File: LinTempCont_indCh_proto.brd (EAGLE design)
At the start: 76.2 x 34.3 mm, 26 parts

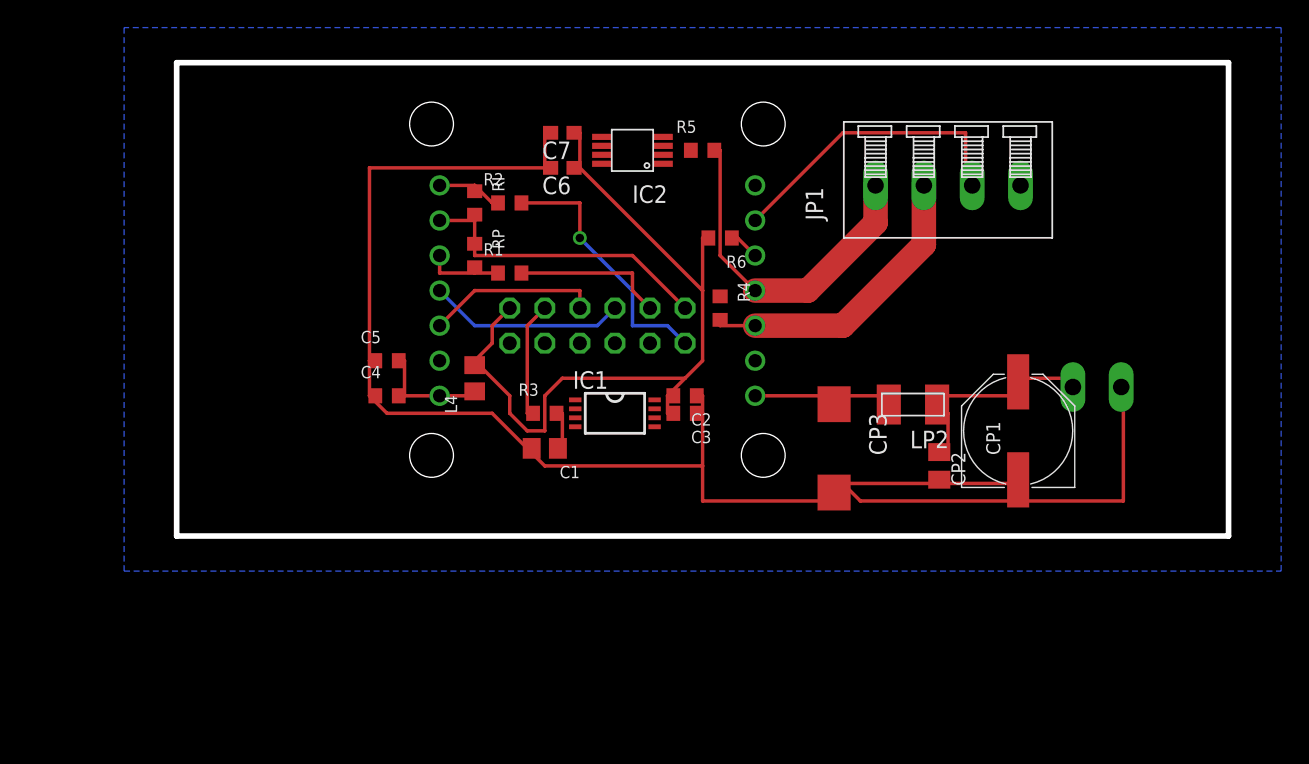
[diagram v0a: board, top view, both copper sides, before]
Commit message: Schematic updates and progress routing both boards
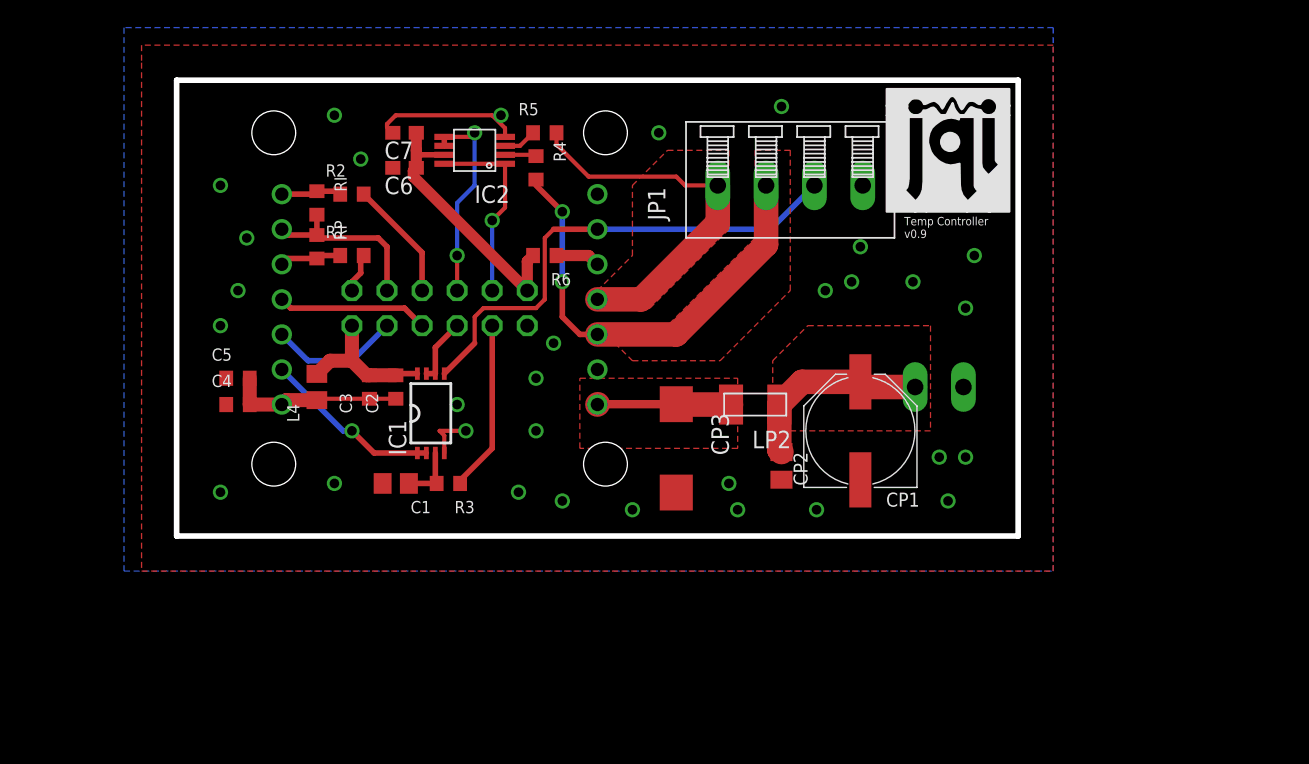
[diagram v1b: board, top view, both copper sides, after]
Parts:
- added U$1: (no value), JQI_Logo:JQI_LOGO_NEGATIVE-SILKSCREEN
- moved C3 22.9 mm to (14.0, 10.8), turned to 90 degrees
- moved C2 21.0 mm to (15.9, 10.8), turned to 90 degrees
- moved R4 16.8 mm to (26.0, 26.7)
- moved IC1 13.3 mm to (18.4, 8.89), turned to 90 degrees
- moved R6 12.8 mm to (26.7, 20.3)
- moved JP3 11.5 mm to (19.1, 16.5)
- moved R1 11.5 mm to (12.7, 20.3)
- moved R5 11.5 mm to (26.7, 29.2)
- moved L4 11.4 mm to (10.2, 10.8)
- moved R2 11.4 mm to (12.7, 24.8)
- moved RP 11.4 mm to (10.2, 21.0)
- moved U1 11.4 mm to (19.1, 17.1)
- moved LP2 11.4 mm to (41.9, 9.53)
- moved IC2 11.4 mm to (21.6, 27.9)
- moved C6 11.4 mm to (16.5, 26.7)
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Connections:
- net +1V: now also JP3.3; no longer JP3.11
- net 2.5V: now also JP3.9; no longer JP3.10
- net ACT_T: now also JP3.8; no longer JP3.6
- net AGND: now also JP3.12; no longer JP3.2
- net I: now also JP3.5; no longer JP3.12
- net LIMA: now also JP3.4; no longer JP3.5
- net LIMB: now also JP3.6; no longer JP3.7
- net P: now also JP3.1; no longer JP3.9
- net VDD: now also JP3.11, JP3.2; no longer JP3.1
- net VMON: now also JP3.7; no longer JP3.8
- net VSET: now also JP3.10; no longer JP3.3
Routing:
- net AGND: track 121.3 -> 20.1 mm, vias 0 -> 31
- net VDD: track 57.3 -> 30.5 mm
- net VMON: track 0.00 -> 14.9 mm, vias 0 -> 2
- net N$2: track 22.2 -> 36.2 mm
- net 2.5V: track 0.00 -> 14.0 mm, vias 0 -> 1
- net N$7: track 0.00 -> 13.0 mm, vias 0 -> 1
- net OUTB: track 21.9 -> 33.0 mm, vias 0 -> 2
- net I: track 19.0 -> 8.74 mm, vias 1 -> 0
- net +1V: track 22.3 -> 12.8 mm
- net P: track 11.1 -> 2.89 mm
- net ACT_T: track 0.00 -> 4.78 mm
- net VSET: track 8.57 -> 12.4 mm
- net LIMB: track 14.3 -> 10.9 mm
- net LIMA: track 12.5 -> 9.46 mm
- net N$16: track 0.00 -> 2.42 mm
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- added copper zone on layer 1, net AGND
- added copper zone on layer 1, net OUTA
- added copper zone on layer 1, net OUTB
- added copper zone on layer 1, net V+
- added copper zone on layer 1, net VSS
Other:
- board size 76.2 x 34.3 mm -> 61 x 33 mm
- board text added: "Temp Controller v0.9"

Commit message: Board/Schematic updates and tweaks
Incorporate suggestions from Neal and Alessandro
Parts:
- added C8: 100nF, rlc-jqi:0603
- added RSG: DNP, rlc-jqi:0603
- R6: device rlc-jqi:0603 -> jqi_passives:R_0805
- moved RI 6.38 mm to (3.81, 24.8)
- moved RP 6.38 mm to (3.81, 20.3)
- moved R1 0.90 mm to (12.1, 21.0)
- moved R2 0.63 mm to (12.1, 24.8)
- moved R6 0.63 mm to (26.7, 21.0)
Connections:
- new net N$6: RSG.2, U1.P$8
- net AGND: now also C8.1, RSG.1
- net N$2: now also C8.2
- net N$4: now also R6.P$1; no longer R6.1
- net VDD: now also R6.P$2; no longer R6.2
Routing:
- net +1V: track 12.8 -> 19.1 mm
- net N$2: track 36.2 -> 41.1 mm
- net AGND: track 20.1 -> 15.5 mm
- net N$3: track 4.41 -> 8.72 mm
- net N$1: track 4.49 -> 8.59 mm
- net I: track 8.74 -> 10.7 mm
- net VDD: track 30.5 -> 31.1 mm
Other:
- board text added: "Temp Controller v0.9 BJR"
- board text removed: "Temp Controller v0.9"

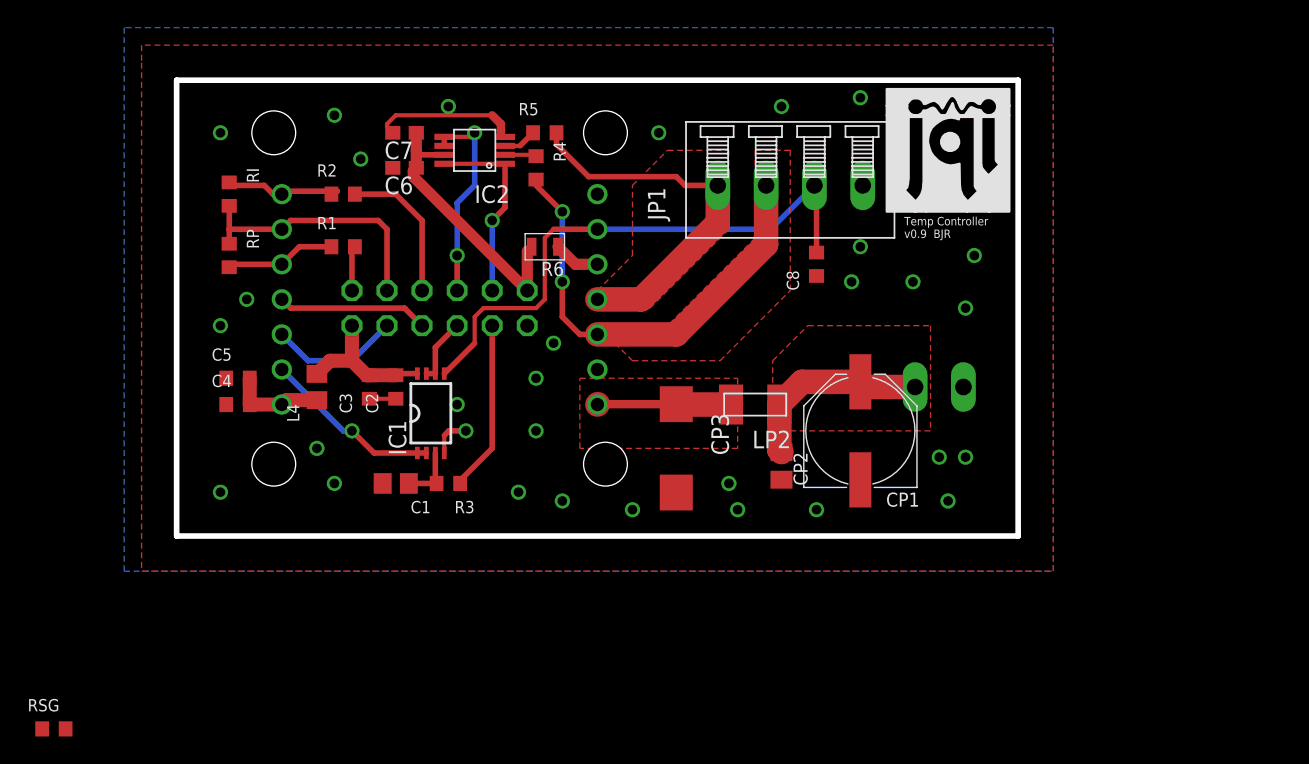
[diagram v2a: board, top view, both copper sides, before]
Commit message: Board/Schematic Clean up-lcd.init tweak
Added encoder hold event to initialize LCD to try to get around bug
where LCD display goes blank. The bug appears to be from a loose solder
connection on first prototype
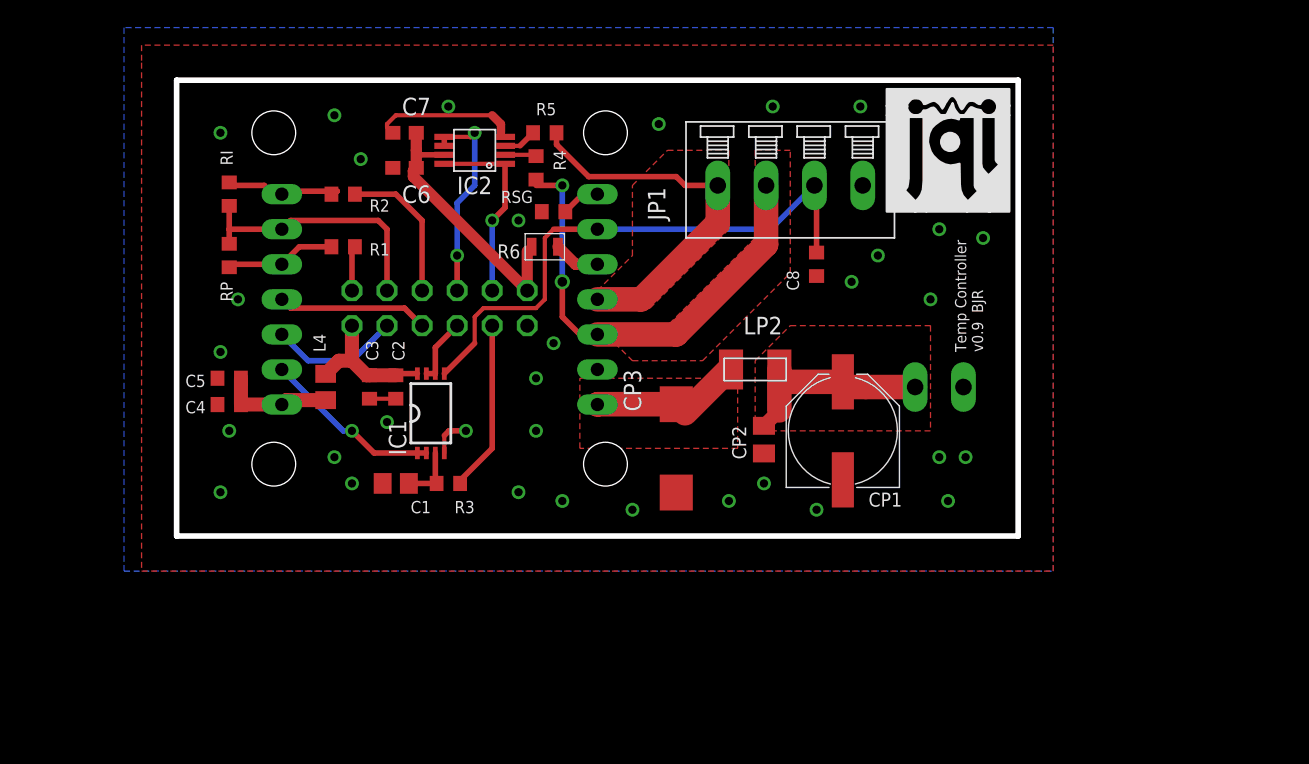
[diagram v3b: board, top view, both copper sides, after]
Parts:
- moved RSG 52.1 mm to (27.3, 23.5)
- moved LP2 2.54 mm to (41.9, 12.1)
- moved CP2 2.29 mm to (42.5, 6.99)
- moved CP1 1.27 mm to (48.3, 7.62)
- moved C4 0.64 mm to (3.81, 9.53)
- moved C5 0.64 mm to (3.81, 11.4)
- moved L4 0.63 mm to (10.8, 10.8)
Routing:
- net N$6: track 0.00 -> 2.85 mm
- net VSS: track 9.70 -> 11.3 mm
- net N$26: track 6.90 -> 8.17 mm
- net OUTB: track 33.0 -> 34.1 mm
- net V+: track 14.2 -> 14.9 mm
- net VDD: track 31.1 -> 30.5 mm
- net AGND: vias 31 -> 33

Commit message: Add DAC Vref Jumper/Silkscreen Cleanup
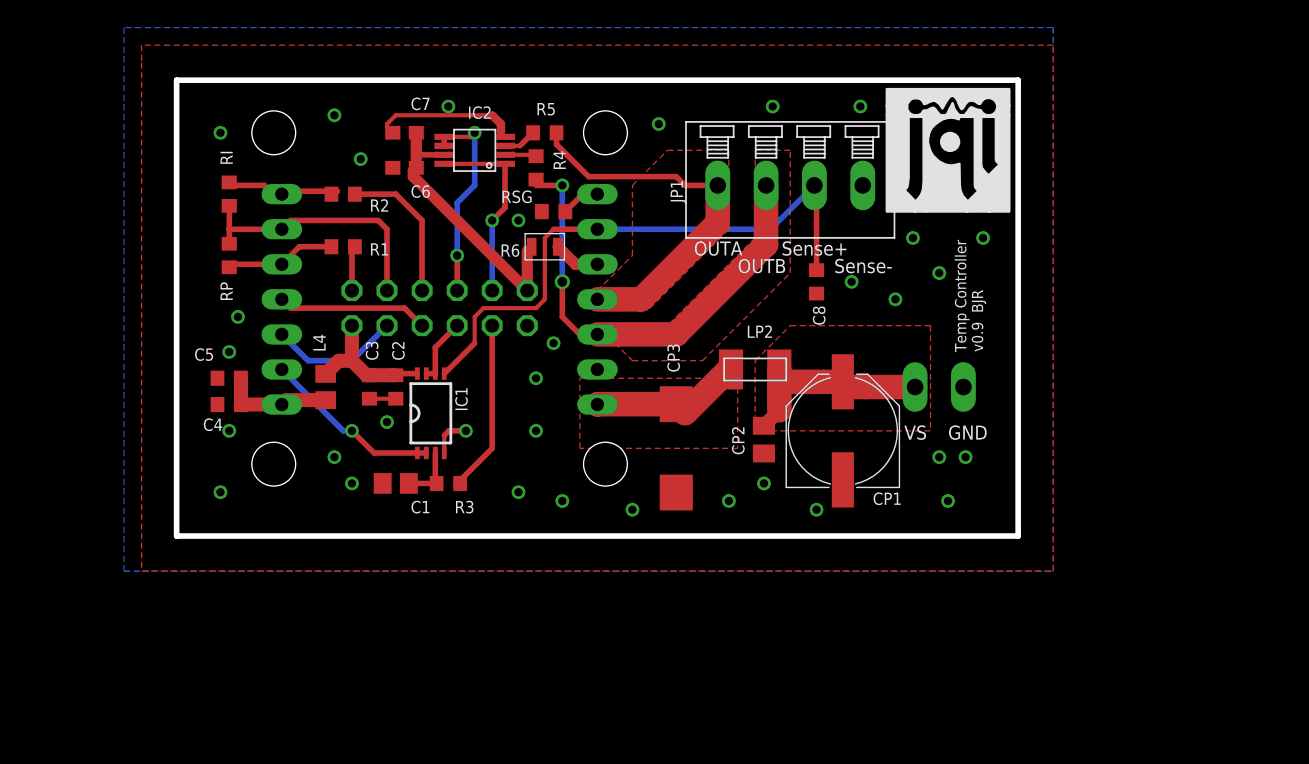
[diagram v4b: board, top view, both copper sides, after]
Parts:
- moved C8 1.27 mm to (46.4, 18.4)
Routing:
- net N$2: track 41.1 -> 42.4 mm
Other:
- board text added: "GND"
- board text added: "OUTA"
- board text added: "OUTB"
- board text added: "Sense+"
- board text added: "Sense-"
- board text added: "VS"

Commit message: Add BOM, minor updates to reflect part availability
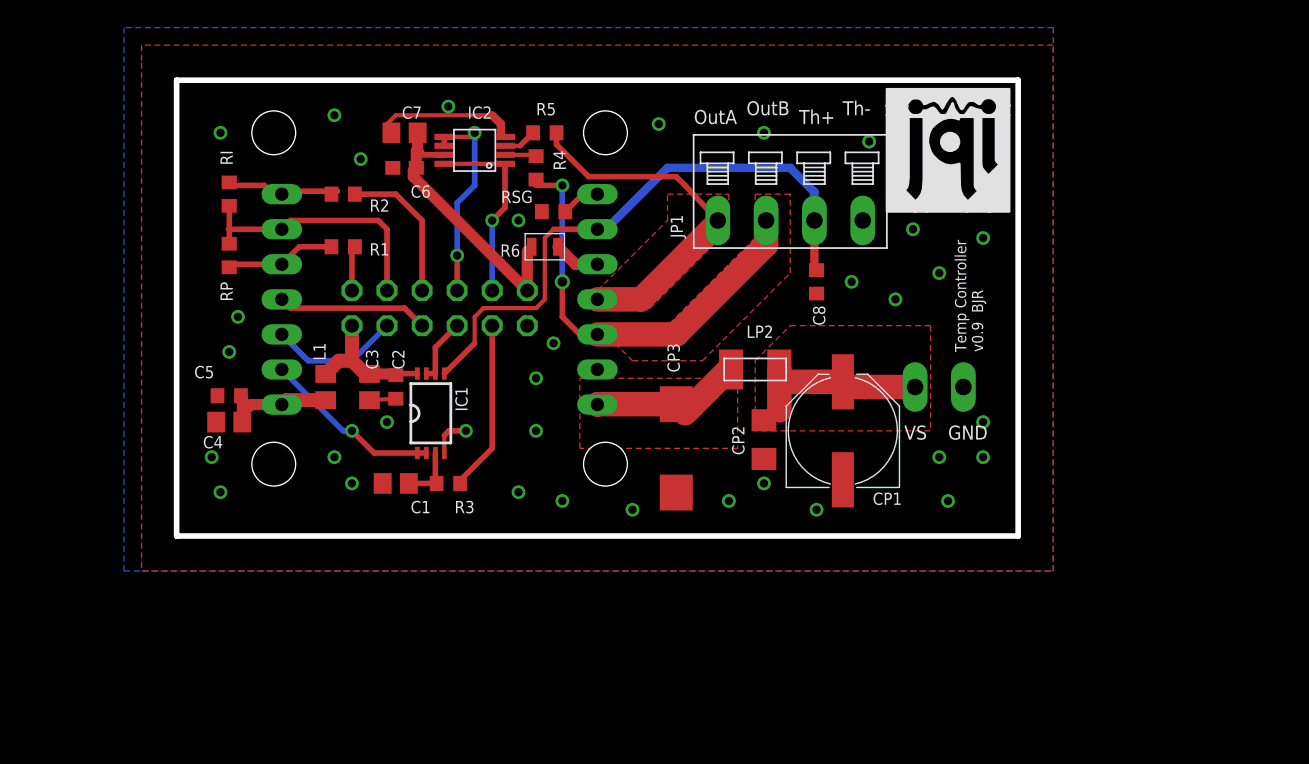
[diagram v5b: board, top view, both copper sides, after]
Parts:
- C3, C4: device rlc-jqi:0603 -> rlc-jqi:0805
- C7: device rcl:C0603 -> rcl:C0805
- C8: value 100nF -> 0.1uF
- CP2: value 10uF -> 10uF 50V; device rcl:C0805K -> rcl:C1206
- JP1: device Lin-Temp-Controller:1X04_RA_SCRWTRM -> Lin-Temp-Controller:1X04_RA_SCRWTRM_ED550
- JP2: device Lin-Temp-Controller:1X02_RA_SCRWTRM -> Lin-Temp-Controller:1X02_RA_SCRWTRM_ED550
- R6: value 20k 1% -> 20k 0.1%
- moved JP1 2.54 mm to (44.5, 22.9)
- moved C4 1.27 mm to (3.81, 8.26)
- moved C5 1.27 mm to (3.81, 10.2)
- renumbered L4 to L1
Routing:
- net OUTB: track 34.1 -> 31.6 mm
- net OUTA: track 27.5 -> 26.0 mm
- net N$2: track 42.4 -> 43.2 mm
- net AGND: vias 33 -> 34
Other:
- board text added: "OutA"
- board text added: "OutB"
- board text added: "Th+"
- board text added: "Th-"
- board text removed: "OUTA"
- board text removed: "OUTB"
- board text removed: "Sense+"
- board text removed: "Sense-"

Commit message: Prepare for ordering boards
Update BOM, minor changes to board to move header slightly, ensure
silkscreen is using vector fonts
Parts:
- moved JP1 1.27 mm to (44.5, 21.6)
- moved C8 0.64 mm to (47.0, 18.4), turned to 180 degrees
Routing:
- net N$2: track 43.2 -> 41.8 mm
- net OUTA: track 26.0 -> 25.0 mm
- net OUTB: track 31.6 -> 31.1 mm
